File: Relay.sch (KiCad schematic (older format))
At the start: 11 parts, among them K1 RELAY, Q1 2N3904, U1 OPTO_TRANSISTOR

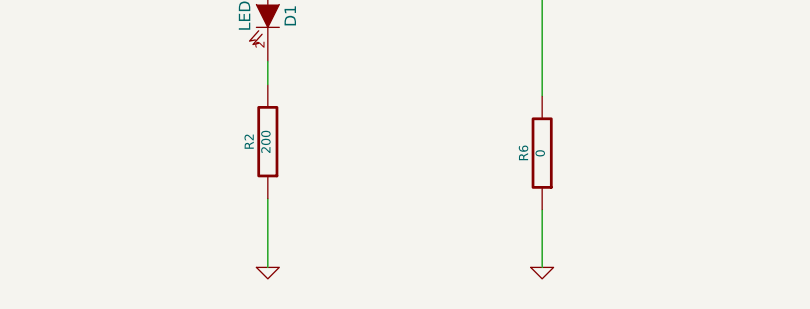
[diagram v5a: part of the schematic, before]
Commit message: Layout v4.0
Adding ground planes according to location of modules
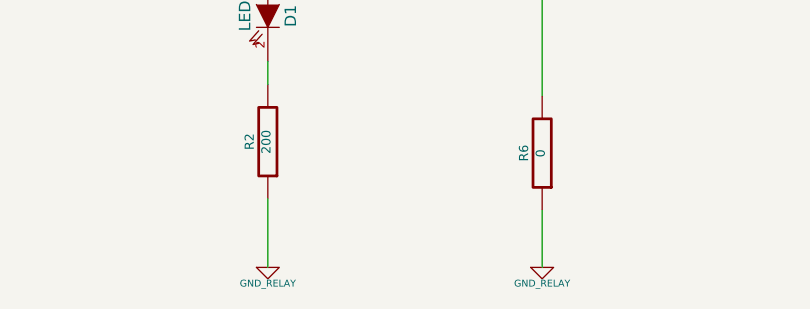
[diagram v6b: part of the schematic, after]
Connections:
- net GND renamed GND_RELAY
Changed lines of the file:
@@
 Sheet 7 9
 Title ""
-Date "3 mar 2014"
+Date "6 mar 2014"
 Rev ""
 Comp ""
@@
 	-1   0    0    1
 $EndComp
-$Comp
-L GND #PWR049
-U 1 1 52F744DA
-P 7850 5400
-F 0 "#PWR049" H 7850 5400 30  0001 C CNN
-F 1 "GND" H 7850 5330 30  0001 C CNN
-F 2 "" H 7850 5400 60  0000 C CNN
-F 3 "" H 7850 5400 60  0000 C CNN
-	1    7850 5400
-	1    0    0    -1
-$EndComp
 Wire Wire Line
 	7850 5400 7850 5150
@@
 Wire Wire Line
 	6650 4500 6650 4600
-$Comp
-L GND #PWR050
-U 1 1 52F7451F
-P 6650 5400
-F 0 "#PWR050" H 6650 5400 30  0001 C CNN
-F 1 "GND" H 6650 5330 30  0001 C CNN
-F 2 "" H 6650 5400 60  0000 C CNN
-F 3 "" H 6650 5400 60  0000 C CNN
-	1    6650 5400
-	1    0    0    -1
-$EndComp
 Wire Wire Line
 	6650 5400 6650 5100
 $Comp
-L +12V #PWR051
+L +12V #PWR049
 U 1 1 52F74537
 P 7400 2050
-F 0 "#PWR051" H 7400 2000 20  0001 C CNN
+F 0 "#PWR049" H 7400 2000 20  0001 C CNN
 F 1 "+12V" H 7400 2150 30  0000 C CNN
 F 2 "" H 7400 2050 60  0000 C CNN
@@
 	7850 2150 7400 2150
 Connection ~ 7400 2150
+$Comp
+L GND_RELAY #PWR050
+U 1 1 531841BF
+P 6650 5400
+F 0 "#PWR050" H 6650 5400 30  0001 C CNN
+F 1 "GND_RELAY" H 6650 5330 30  0000 C CNN
+F 2 "" H 6650 5400 60  0000 C CNN
+F 3 "" H 6650 5400 60  0000 C CNN
+	1    6650 5400
+	1    0    0    -1
+$EndComp
+$Comp
+L GND_RELAY #PWR051
+U 1 1 531841CE
+P 7850 5400
+F 0 "#PWR051" H 7850 5400 30  0001 C CNN
+F 1 "GND_RELAY" H 7850 5330 30  0000 C CNN
+F 2 "" H 7850 5400 60  0000 C CNN
+F 3 "" H 7850 5400 60  0000 C CNN
+	1    7850 5400
+	1    0    0    -1
+$EndComp
 $EndSCHEMATC
